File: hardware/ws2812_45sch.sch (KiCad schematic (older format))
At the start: 64 parts

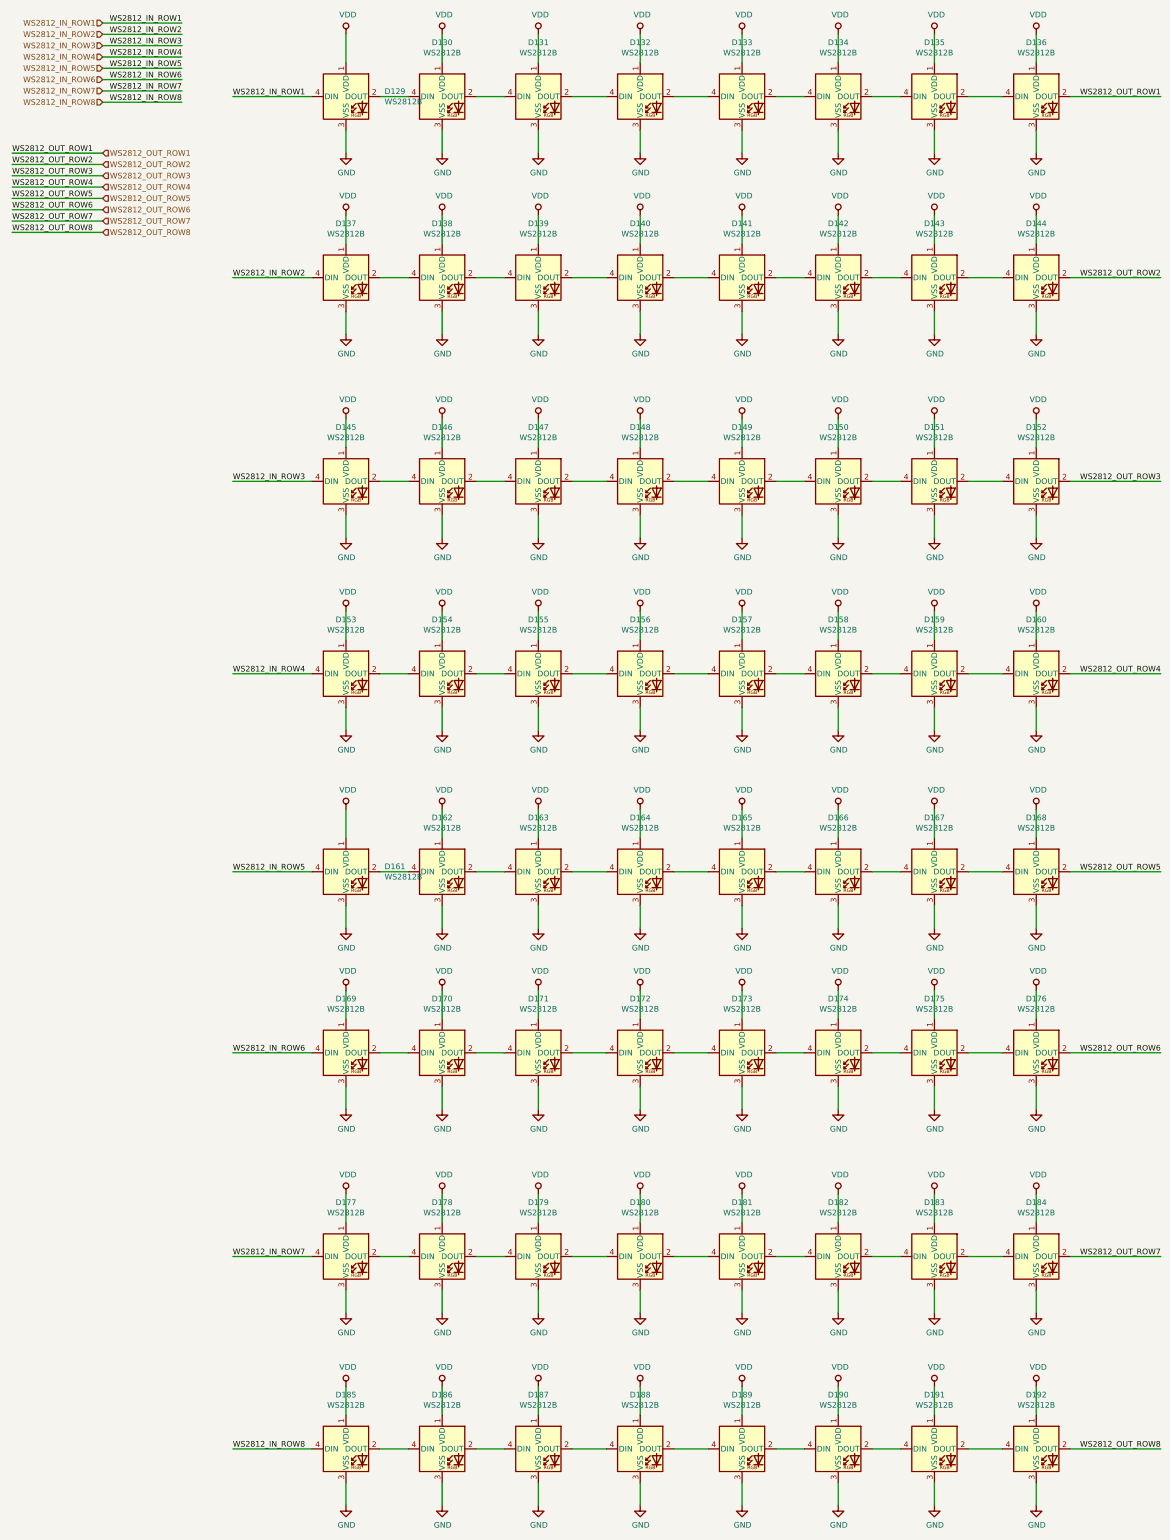
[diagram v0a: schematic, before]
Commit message: update WS2812\,
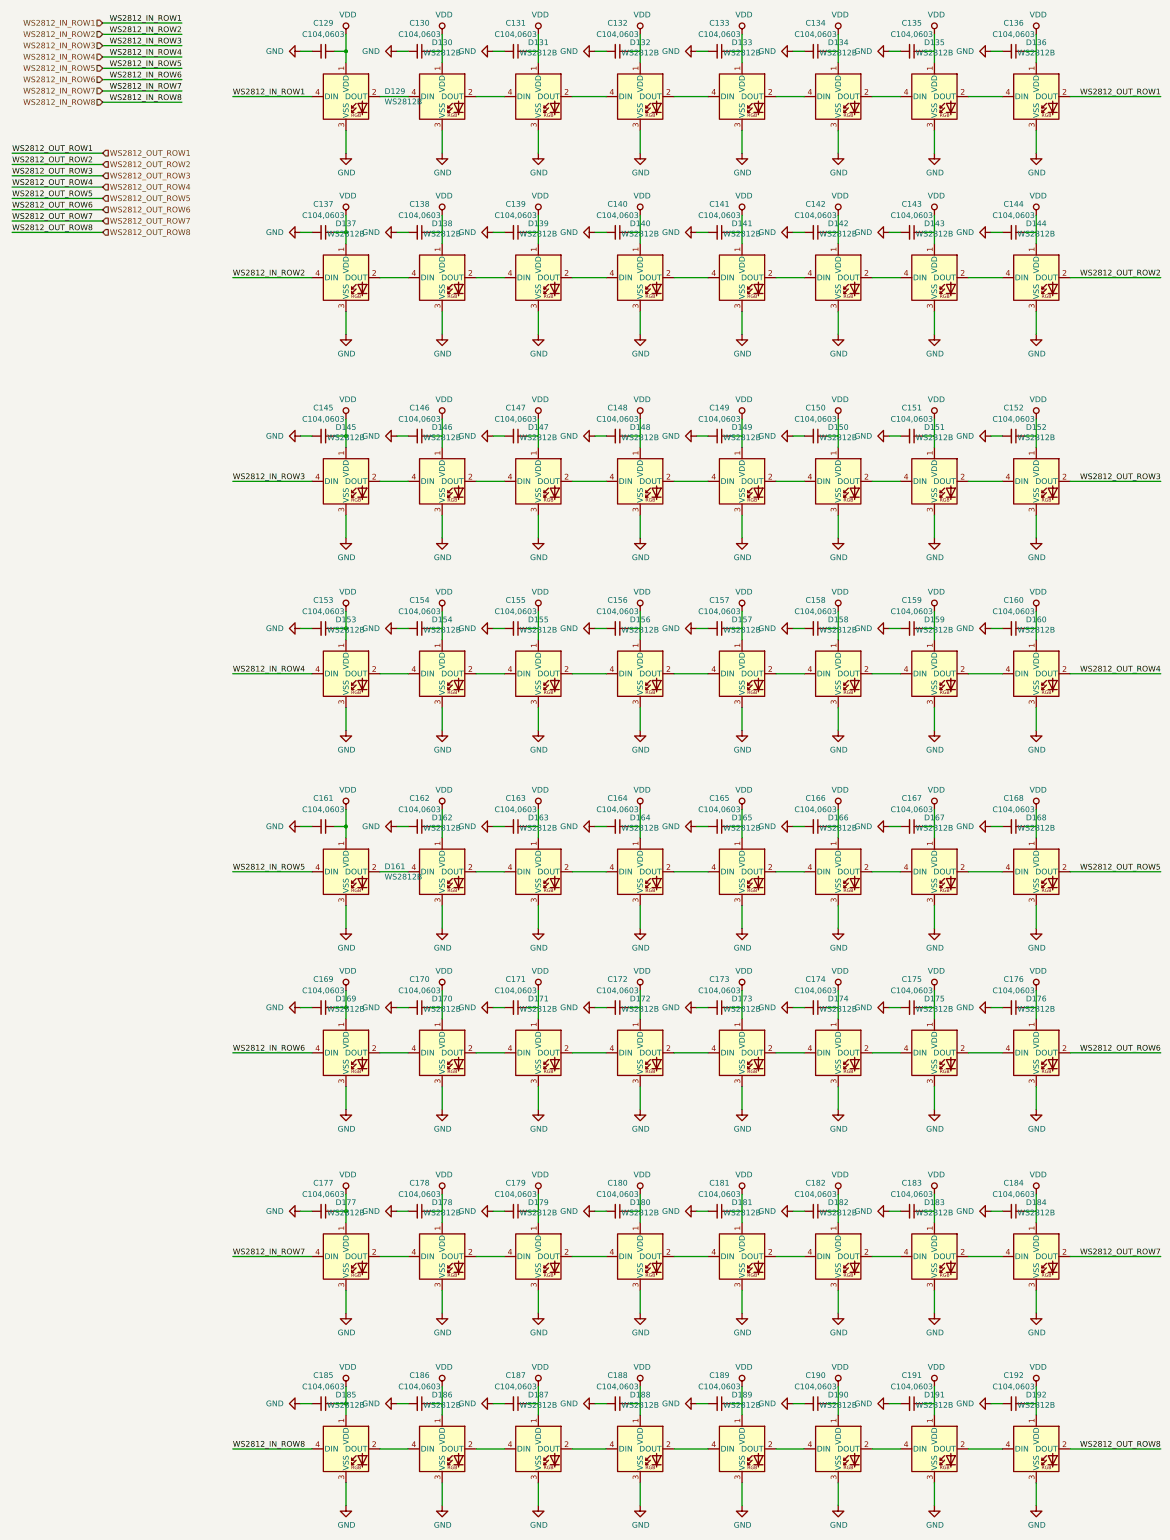
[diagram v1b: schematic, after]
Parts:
- added C129, C130, C131, C132, C133, C134, C135, C136, C137, C138, C139, C140, C141, C142, C143, C144, C145, C146, C147, C148, C149, C150, C151, C152, C153, C154, C155, C156, C157, C158, C159, C160, C161, C162, C163, C164, C165, C166, C167, C168, C169, C170, C171, C172, C173, C174, C175, C176, C177, C178, C179, C180, C181, C182, C183, C184, C185, C186, C187, C188, C189, C190, C191, C192: C104,0603, Capacitor_SMD:C_0603_1608Metric_Pad1.05x0.95mm_HandSolder, symbol taobao-c:C104,0603
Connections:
- wire segments 216 -> 352
